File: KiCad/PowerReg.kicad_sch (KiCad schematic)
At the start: 5 parts, among them U1 TPS62162DSG

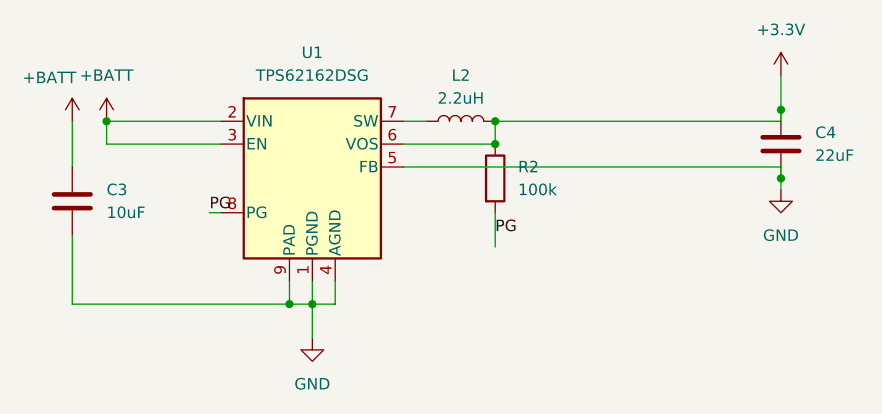
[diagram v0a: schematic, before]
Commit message: Reset all annotationss
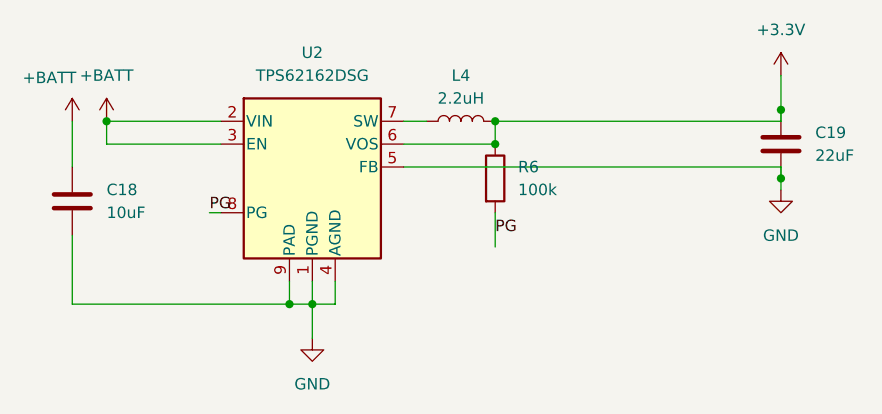
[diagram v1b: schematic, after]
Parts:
- renumbered C3 to C18, C4 to C19, L2 to L4, R2 to R6, U1 to U2
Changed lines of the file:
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@@
 		(dnp no)
 		(fields_autoplaced yes)
-		(property "Reference" "R2"
+		(property "Reference" "R6"
 			(at 146.05 62.2299 0)
 			(effects
@@
 			(project "PowerReg"
 				(path "/16f8cce7-467e-4342-b55a-00af81cd6f69/bf62daab-1cf5-4742-a85c-ffd3166ecdf9"
-					(reference "R2")
+					(reference "R6")
 					(unit 1)
 				)
@@
 		(dnp no)
 		(fields_autoplaced yes)
-		(property "Reference" "#PWR01"
+		(property "Reference" "#PWR036"
 			(at 175.26 55.88 0)
 			(effects
@@
 			(project ""
 				(path "/16f8cce7-467e-4342-b55a-00af81cd6f69/bf62daab-1cf5-4742-a85c-ffd3166ecdf9"
-					(reference "#PWR01")
+					(reference "#PWR036")
 					(unit 1)
 				)
@@
 		(on_board yes)
 		(dnp no)
-		(property "Reference" "#PWR02"
+		(property "Reference" "#PWR033"
 			(at 96.52 60.96 0)
 			(effects
@@
 			(project ""
 				(path "/16f8cce7-467e-4342-b55a-00af81cd6f69/bf62daab-1cf5-4742-a85c-ffd3166ecdf9"
-					(reference "#PWR02")
+					(reference "#PWR033")
 					(unit 1)
 				)
@@
 		(dnp no)
 		(fields_autoplaced yes)
-		(property "Reference" "U1"
+		(property "Reference" "U2"
 			(at 123.19 49.53 0)
 			(effects
@@
 			(project ""
 				(path "/16f8cce7-467e-4342-b55a-00af81cd6f69/bf62daab-1cf5-4742-a85c-ffd3166ecdf9"
-					(reference "U1")
+					(reference "U2")
 					(unit 1)
 				)
@@
 		(dnp no)
 		(fields_autoplaced yes)
-		(property "Reference" "L2"
+		(property "Reference" "L4"
 			(at 139.7 52.07 90)
 			(effects
@@
 			(project "PowerReg"
 				(path "/16f8cce7-467e-4342-b55a-00af81cd6f69/bf62daab-1cf5-4742-a85c-ffd3166ecdf9"
-					(reference "L2")
+					(reference "L4")
 					(unit 1)
 				)
@@
 		(dnp no)
 		(fields_autoplaced yes)
-		(property "Reference" "C3"
+		(property "Reference" "C18"
 			(at 100.33 64.7699 0)
 			(effects
@@
 			(project "PowerReg"
 				(path "/16f8cce7-467e-4342-b55a-00af81cd6f69/bf62daab-1cf5-4742-a85c-ffd3166ecdf9"
-					(reference "C3")
+					(reference "C18")
 					(unit 1)
 				)
@@
 		(dnp no)
 		(fields_autoplaced yes)
-		(property "Reference" "#PWR05"
+		(property "Reference" "#PWR037"
 			(at 175.26 71.12 0)
 			(effects
@@
 			(project "PowerReg"
 				(path "/16f8cce7-467e-4342-b55a-00af81cd6f69/bf62daab-1cf5-4742-a85c-ffd3166ecdf9"
-					(reference "#PWR05")
+					(reference "#PWR037")
 					(unit 1)
 				)
@@
 		(dnp no)
 		(fields_autoplaced yes)
-		(property "Reference" "#PWR04"
+		(property "Reference" "#PWR034"
 			(at 100.33 60.96 0)
 			(effects
@@
 			(project ""
 				(path "/16f8cce7-467e-4342-b55a-00af81cd6f69/bf62daab-1cf5-4742-a85c-ffd3166ecdf9"
-					(reference "#PWR04")
+					(reference "#PWR034")
 					(unit 1)
 				)
@@
 		(dnp no)
 		(fields_autoplaced yes)
-		(property "Reference" "C4"
+		(property "Reference" "C19"
 			(at 179.07 58.4199 0)
 			(effects
@@
 			(project "PowerReg"
 				(path "/16f8cce7-467e-4342-b55a-00af81cd6f69/bf62daab-1cf5-4742-a85c-ffd3166ecdf9"
-					(reference "C4")
+					(reference "C19")
 					(unit 1)
 				)
@@
 		(dnp no)
 		(fields_autoplaced yes)
-		(property "Reference" "#PWR03"
+		(property "Reference" "#PWR035"
 			(at 123.19 87.63 0)
 			(effects
@@
 			(project ""
 				(path "/16f8cce7-467e-4342-b55a-00af81cd6f69/bf62daab-1cf5-4742-a85c-ffd3166ecdf9"
-					(reference "#PWR03")
-					(unit 1)
-				)
+					(reference "#PWR035")
+					(unit 1)
+				)

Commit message: Updated several footprints
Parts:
- C18, C19: footprint Capacitor_SMD:C_0201_0603Metric -> Capacitor_SMD:C_0603_1608Metric
- L4: footprint Inductor_SMD:L_1008_2520Metric -> (none)
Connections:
- net +3.3V renamed +3V3

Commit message: All footprints placed
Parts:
- L4: footprint (none) -> NR3015T:IND_TAIYO_NR3015_TAY
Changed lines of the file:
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@@
 			)
 		)
-		(property "Footprint" ""
+		(property "Footprint" "NR3015T:IND_TAIYO_NR3015_TAY"
 			(at 139.7 57.15 0)
 			(effects
